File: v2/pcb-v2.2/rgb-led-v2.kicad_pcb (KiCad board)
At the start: 2 copper layers, 90 x 50 mm, 22 parts, among them CON1 BARREL_JACK, P1 CONN_01X15, P2 CONN_01X15, SW1 SPST

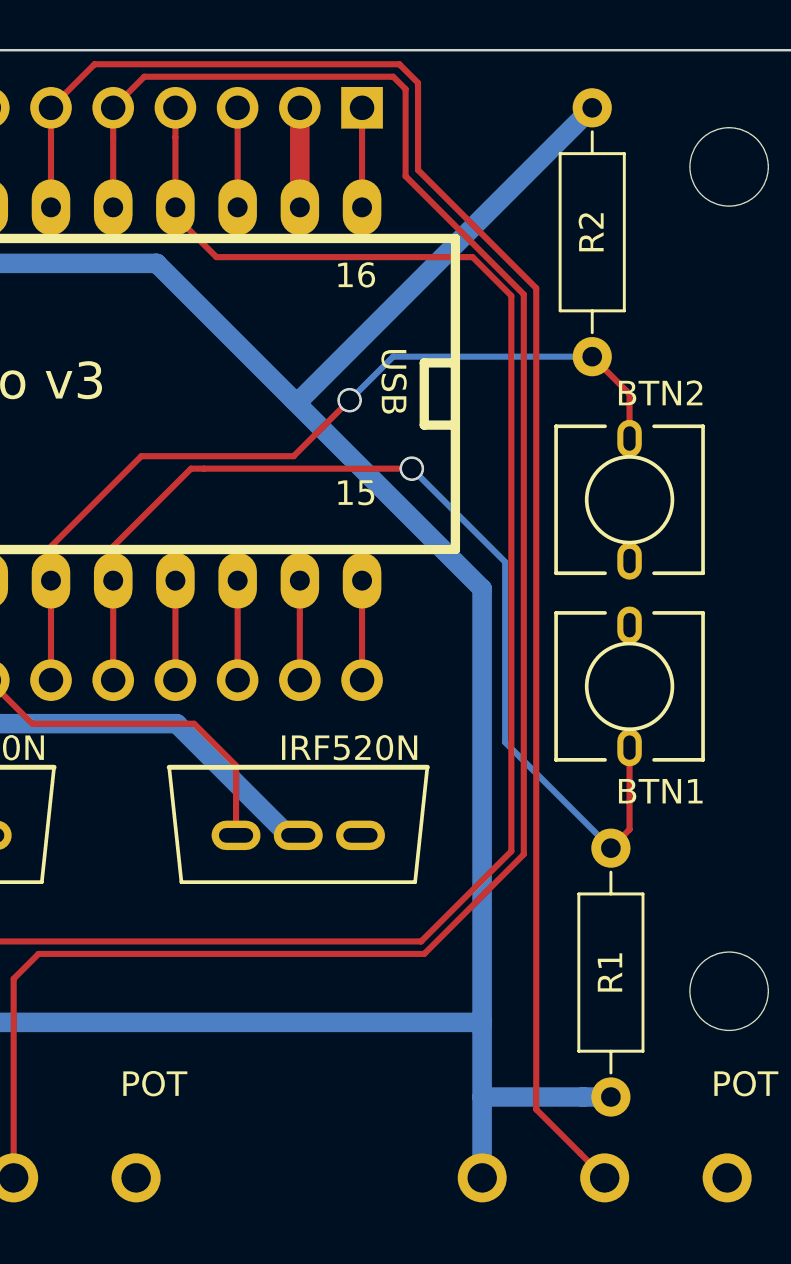
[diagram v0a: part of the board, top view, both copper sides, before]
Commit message: Align resistors
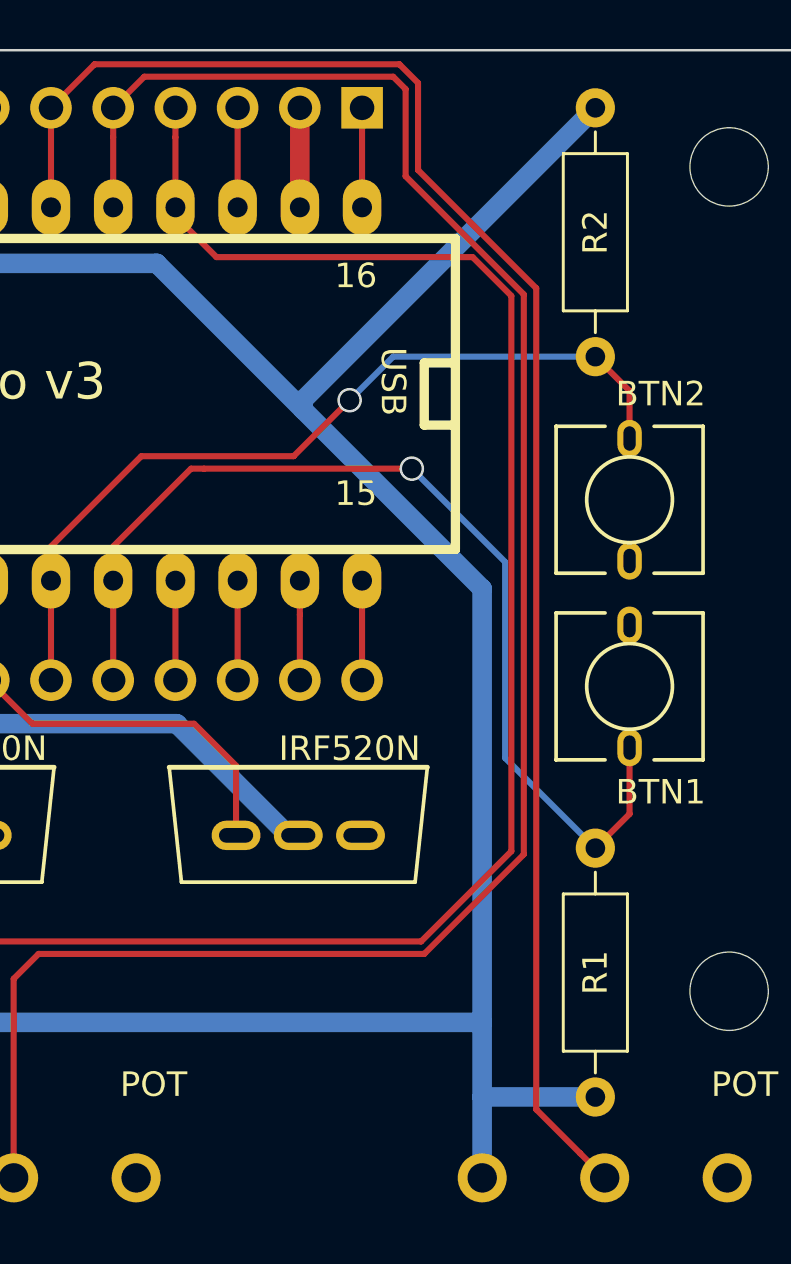
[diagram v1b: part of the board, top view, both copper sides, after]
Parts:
- moved R1 0.63 mm to (97.4, 52.6)
- moved R2 0.13 mm to (97.4, 32.5)
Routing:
- net 5V: track 147.3 -> 146.8 mm

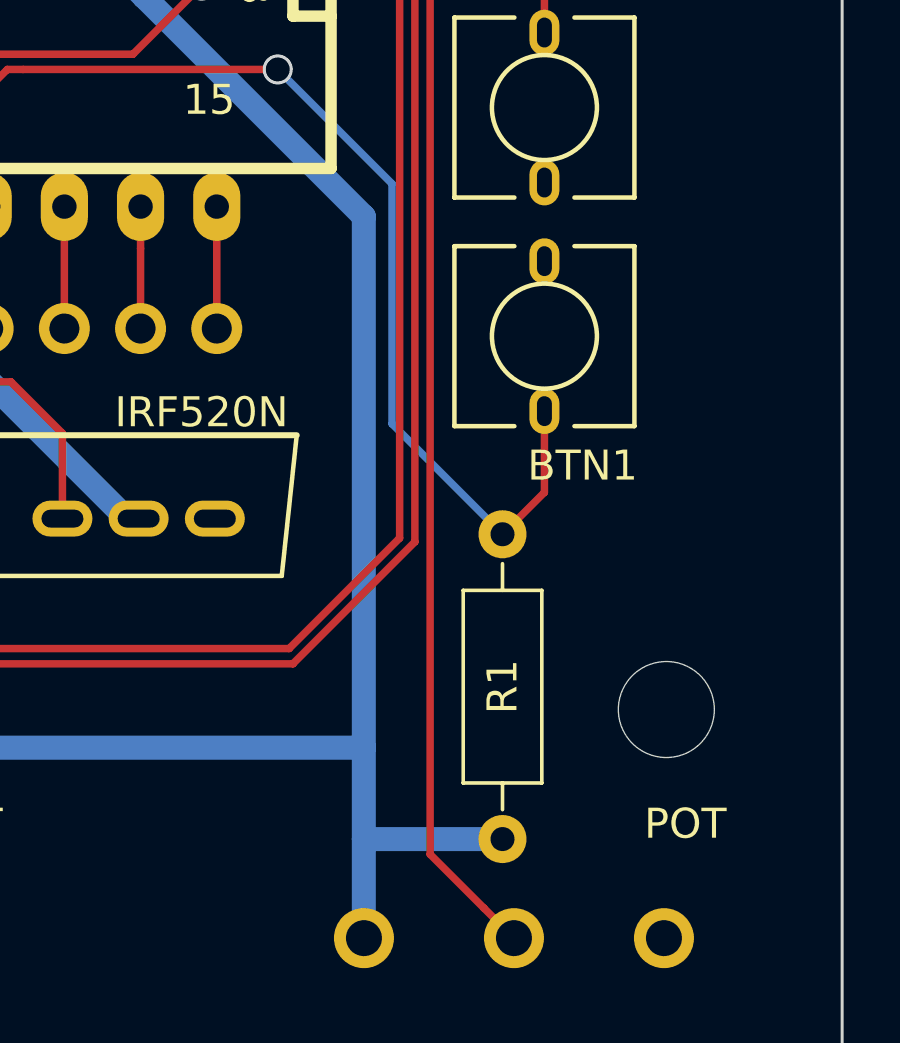
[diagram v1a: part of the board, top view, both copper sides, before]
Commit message: More resistor alignment
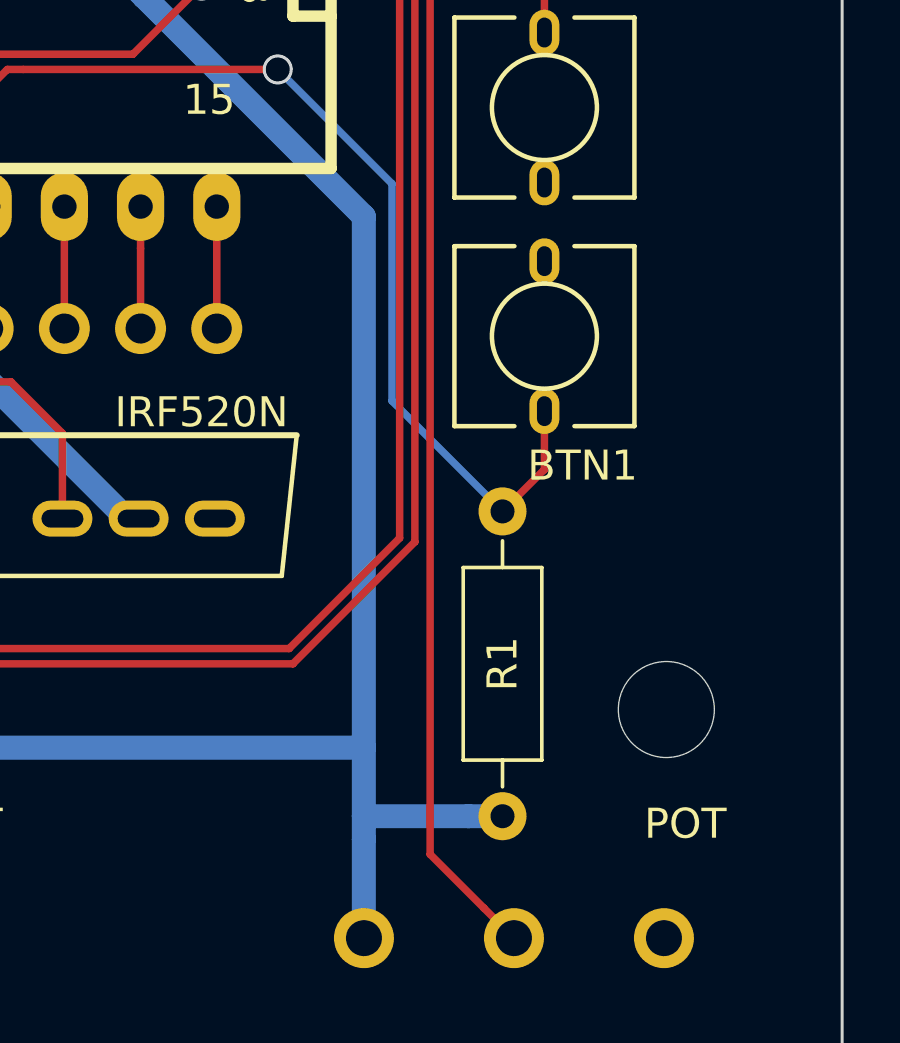
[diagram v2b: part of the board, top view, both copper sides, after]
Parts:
- moved R1 0.76 mm to (97.4, 51.8)
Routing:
- net A26: track 42.2 -> 40.7 mm
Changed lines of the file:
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@@
     (thickness 1.6)
     (drawings 31)
-    (tracks 154)
+    (tracks 156)
     (zones 0)
     (modules 22)
@@
   )
   (module Resistors_THT:R_Axial_DIN0207_L6.3mm_D2.5mm_P10.16mm_Horizontal (layer F.Cu)
-    (at 97.409 52.578 270)
+    (at 97.409 51.816 270)
     (descr "Resistor, Axial_DIN0207 series, Axial, Horizontal, pin pitch=10.16mm, 0.25W = 1/4W, length*diameter=6.3*2.5mm^2, http://cdn-reichelt.de/documents/datenblatt/B400/1_4W%23YAG.pdf")
     (tags "Resistor Axial_DIN0207 series Axial Horizontal pin pitch 10.16mm 0.25W = 1/4W length 6.3mm diameter 2.5mm")
@@
   (segment (start 65.024 26.416) (end 65.024 22.352) (width 0.25) (layer F.Cu) (net 17))
   (segment (start 62.484 22.352) (end 62.484 26.416) (width 0.25) (layer F.Cu) (net 18))
+  (segment (start 92.7862 59.6938) (end 92.7862 61.976) (width 0.8) (layer B.Cu) (net 19))
+  (segment (start 92.7862 61.976) (end 92.7862 62.738) (width 0.8) (layer B.Cu) (net 19))
+  (segment (start 97.409 61.976) (end 96.27763 61.976) (width 0.8) (layer B.Cu) (net 19))
+  (segment (start 96.27763 61.976) (end 92.7862 61.976) (width 0.8) (layer B.Cu) (net 19))
   (segment (start 79.502 28.702) (end 85.471 34.671) (width 0.8) (layer B.Cu) (net 19))
   (segment (start 85.471 34.671) (end 92.7862 41.9862) (width 0.8) (layer B.Cu) (net 19))
   (segment (start 97.409 22.352) (end 85.471 34.29) (width 0.8) (layer B.Cu) (net 19))
   (segment (start 85.471 34.29) (end 85.471 34.671) (width 0.8) (layer B.Cu) (net 19))
-  (segment (start 97.409 62.738) (end 92.7862 62.738) (width 0.8) (layer B.Cu) (net 19))
   (segment (start 59.944 26.416) (end 59.944 22.352) (width 0.8) (layer F.Cu) (net 19))
   (segment (start 79.502 28.702) (end 61.8744 28.702) (width 0.8) (layer B.Cu) (net 19))
@@
   (segment (start 92.7862 41.9862) (end 92.7862 59.6862) (width 0.8) (layer B.Cu) (net 19))
   (segment (start 92.7862 59.6862) (end 92.79 59.69) (width 0.8) (layer B.Cu) (net 19))
-  (segment (start 92.7862 59.6938) (end 92.7862 62.738) (width 0.8) (layer B.Cu) (net 19))
   (segment (start 92.7862 62.738) (end 92.7862 66.0362) (width 0.8) (layer B.Cu) (net 19))
   (segment (start 68.66 59.69) (end 92.79 59.69) (width 0.8) (layer B.Cu) (net 19))
@@
   (segment (start 89.154 32.512) (end 87.376 34.29) (width 0.25) (layer B.Cu) (net 29))
   (via (at 87.376 34.29) (size 1) (drill 0.8) (layers F.Cu B.Cu) (net 29))
-  (segment (start 98.806 48.474) (end 98.806 51.181) (width 0.25) (layer F.Cu) (net 30))
-  (segment (start 98.806 51.181) (end 97.409 52.578) (width 0.25) (layer F.Cu) (net 30))
+  (segment (start 98.806 48.474) (end 98.806 50.419) (width 0.25) (layer F.Cu) (net 30))
+  (segment (start 98.806 50.419) (end 97.409 51.816) (width 0.25) (layer F.Cu) (net 30))
+  (segment (start 93.726 40.894) (end 93.726 48.133) (width 0.25) (layer B.Cu) (net 30))
+  (segment (start 93.726 48.133) (end 97.409 51.816) (width 0.25) (layer B.Cu) (net 30))
   (segment (start 89.916 37.084) (end 93.726 40.894) (width 0.25) (layer B.Cu) (net 30))
-  (segment (start 93.726 48.895) (end 97.409 52.578) (width 0.25) (layer B.Cu) (net 30))
-  (segment (start 93.726 40.894) (end 93.726 48.895) (width 0.25) (layer B.Cu) (net 30))
   (segment (start 77.724 41.656) (end 77.724 40.263) (width 0.25) (layer F.Cu) (net 30))
   (segment (start 77.724 40.263) (end 80.903 37.084) (width 0.25) (layer F.Cu) (net 30))
